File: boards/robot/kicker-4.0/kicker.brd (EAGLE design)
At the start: 141 x 146.1 mm, 157 parts, among them J1 B2PS-VH(LF)(SN), J2 B2PS-VH(LF)(SN), J3 B2PS-VH(LF)(SN), J4 HFW8R-1ST, J5 2-PIN_2MM-H, J6 3-PIN_2MM-H, J7 !BTN_KCK_PRE_EXT, J8 !BTN_CHP_PRE_EXT, J9 !BTN_CHG_PRE_EXT, Q1 ATP302ATPAK, Q10 BSS806NSOT-23-3, Q2 IRFS4227, Q3 IXGK400N30A3, Q4 IXGK400N30A3, Q5 BSS127, Q6 AOD1N60, Q7 BSS127, Q8 BSS127, Q9 BSS127, T1 DA203X-ALDA2034, U1 MPM3620GQV-P, U2 15V, U3 LT3751FE, U4 IX4427N, U5 AT32ATQFP44, U6 ADUM7441ARQZ-RL7, U7 ADUM7441CRQZ-RL7

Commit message: Fixed buttons
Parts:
- removed J7: !BTN_KCK_PRE_EXT, RoboJackets-Connectors:1X2
- removed J8: !BTN_CHP_PRE_EXT, RoboJackets-Connectors:1X2
- removed J9: !BTN_CHG_PRE_EXT, RoboJackets-Connectors:1X2
- S2, S3, S4: value HDP001R -> KMR2; device RoboJackets-Switches:HDP001R -> RoboJackets-Switches:KMR2
- moved S3 1.12 mm to (68.0, -8.00), turned to 90 degrees
- moved R52 1.00 mm to (57.2, -4.40)
- moved S2 0.71 mm to (68.0, 2.00), turned to 90 degrees
- moved S4 0.71 mm to (68.0, -19.0), turned to 90 degrees
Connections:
- net !BTN_CHG: now also S4.2.1, S4.2.2; no longer J9.1, S4.C
- net !BTN_CHP: now also S2.2.1, S2.2.2; no longer J8.1, S2.C
- net !BTN_KCK: now also S3.2.1, S3.2.2; no longer J7.1, S3.C
- net GND: now also S2.1.1, S2.1.2, S3.1.1, S3.1.2, S4.1.1, S4.1.2; no longer J7.2, J8.2, J9.2, S2.B, S3.B, S4.B
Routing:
- net GND: track 220.2 -> 232.2 mm
- net !BTN_KCK: track 52.6 -> 59.4 mm, vias 3 -> 4
- net !BTN_CHG: track 60.1 -> 66.1 mm, vias 3 -> 4
- net !BTN_CHP: track 28.0 -> 31.3 mm
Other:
- board text added: "18.5V"
- board text removed: "PWR: 16-22V"

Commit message: Pot moved
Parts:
- moved RV1 40.2 mm to (-4.20, 74.5), turned to 0 degrees
- moved Q7 5.83 mm to (-1.80, 69.1)
- moved R48 3.61 mm to (34.0, 61.9)
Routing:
- net N$3: track 1.65 -> 49.7 mm
- net +5V: track 232.7 -> 256.2 mm, vias 6 -> 8
- net !DONE!_RAW: track 270.6 -> 276.0 mm
- net BB_TX_CL: track 6.83 -> 3.58 mm
- net GND: track 232.2 -> 233.4 mm
- net N$37: track 14.3 -> 13.3 mm

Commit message: More fixes
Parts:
- added C39, C40, C41: 0.1uF 25V, rcl:C0603
- J4: value HFW8R-1ST -> SFW8R-1STE1LF; device RoboJackets-Connectors:HFW8R-1ST -> RoboJackets-Connectors:SFW8R-1STE1LF
- R12: value 1.02k 1% -> 1k 0.1%
- R13: value 11.5k 1% -> 11.5k 0.1%
- R14: value 25.5k 1% -> 25.5k 0.1%
- R16: value 7m 1% >1W -> 10m 0.1% >1W
- R18: value 113k 0.1% -> 114k 0.1%
- R19: value 3.0k 0.1% -> 3.12k 0.1%
- R20, R21, R24: value 100k -> 10k
- R22, R23, R25, R28, R29: value 160 -> 1k
- R30: value 270k -> 300k
- R34: value 1.5k 35W -> 1.0k 3.5W
- R46: value ERJ-P06J274V -> ERJ-P06J140V
- XF1: value 15A -> 10A
- moved C34 10.1 mm to (55.6, 36.4), flipped to the bottom, turned to 0 degrees
- moved J4 6.08 mm to (68.0, 33.0)
- moved S1 1.41 mm to (64.0, 52.0)
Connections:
- net !BTN_CHG: now also C41.1
- net !BTN_CHP: now also C39.1
- net !BTN_KCK: now also C40.1
- net !KICKER_SELECT_EXT: now also J4.P$6; no longer J4.5
- net !RESET_EXT: now also J4.P$5; no longer J4.4
- net GND: now also C39.2, C40.2, C41.2
- net GND_LGC_EXT: now also J4.P$4; no longer J4.3
- net MISO_EXT: now also J4.P$9; no longer J4.8
- net MOSI_EXT: now also J4.P$8; no longer J4.7
- net SCK_EXT: now also J4.P$7; no longer J4.6
- net VCC_LGC_EXT: now also J4.P$3; no longer J4.2
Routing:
- net VCC_LGC_EXT: track 35.4 -> 43.2 mm, vias 0 -> 1
- net GND: track 233.4 -> 237.1 mm, vias 372 -> 374
- net !BTN_CHP: track 31.3 -> 34.2 mm
- net !BTN_CHG: track 66.1 -> 68.4 mm
- net !BTN_KCK: track 59.3 -> 61.2 mm
- net !RESET_EXT: track 8.89 -> 7.77 mm
- net GND_LGC_EXT: track 27.9 -> 27.0 mm
- net N$14: track 3.30 -> 3.89 mm
- net +5V: track 256.2 -> 255.6 mm

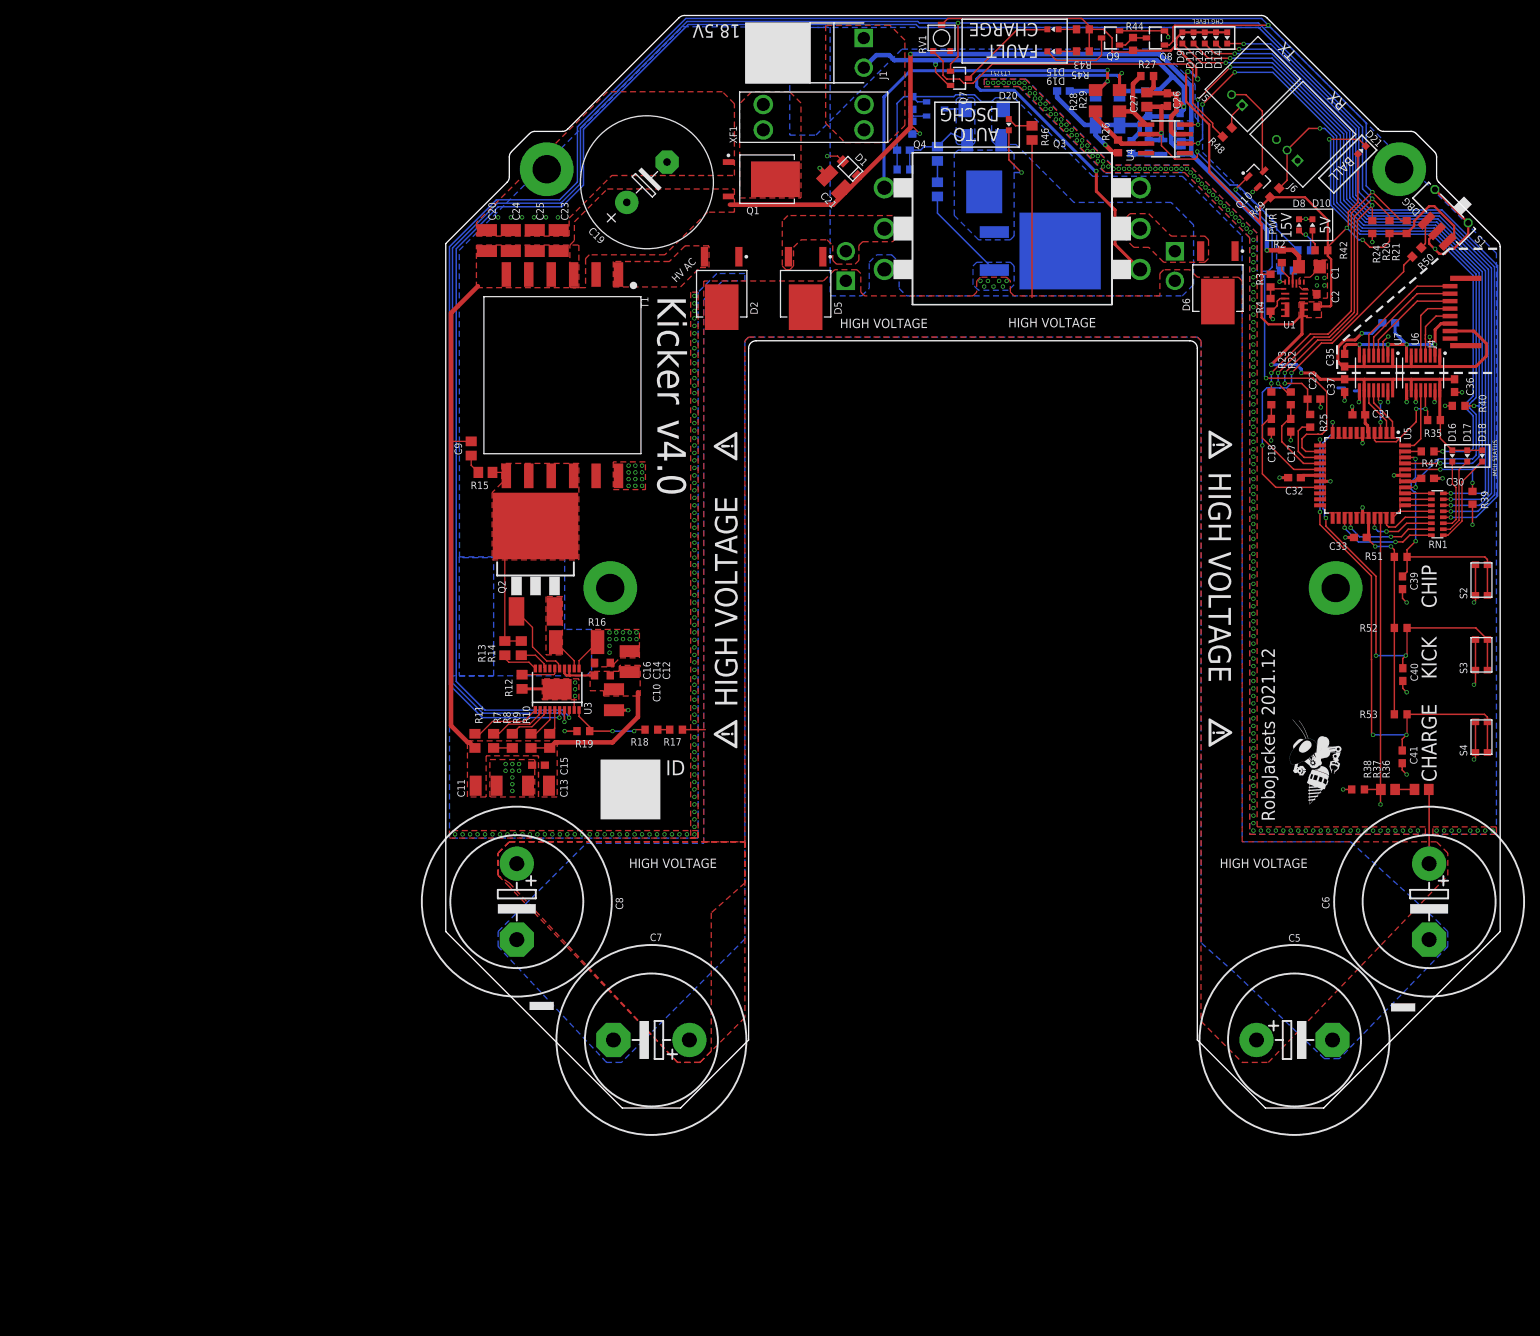
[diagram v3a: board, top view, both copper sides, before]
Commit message: Moved solenoid connectors
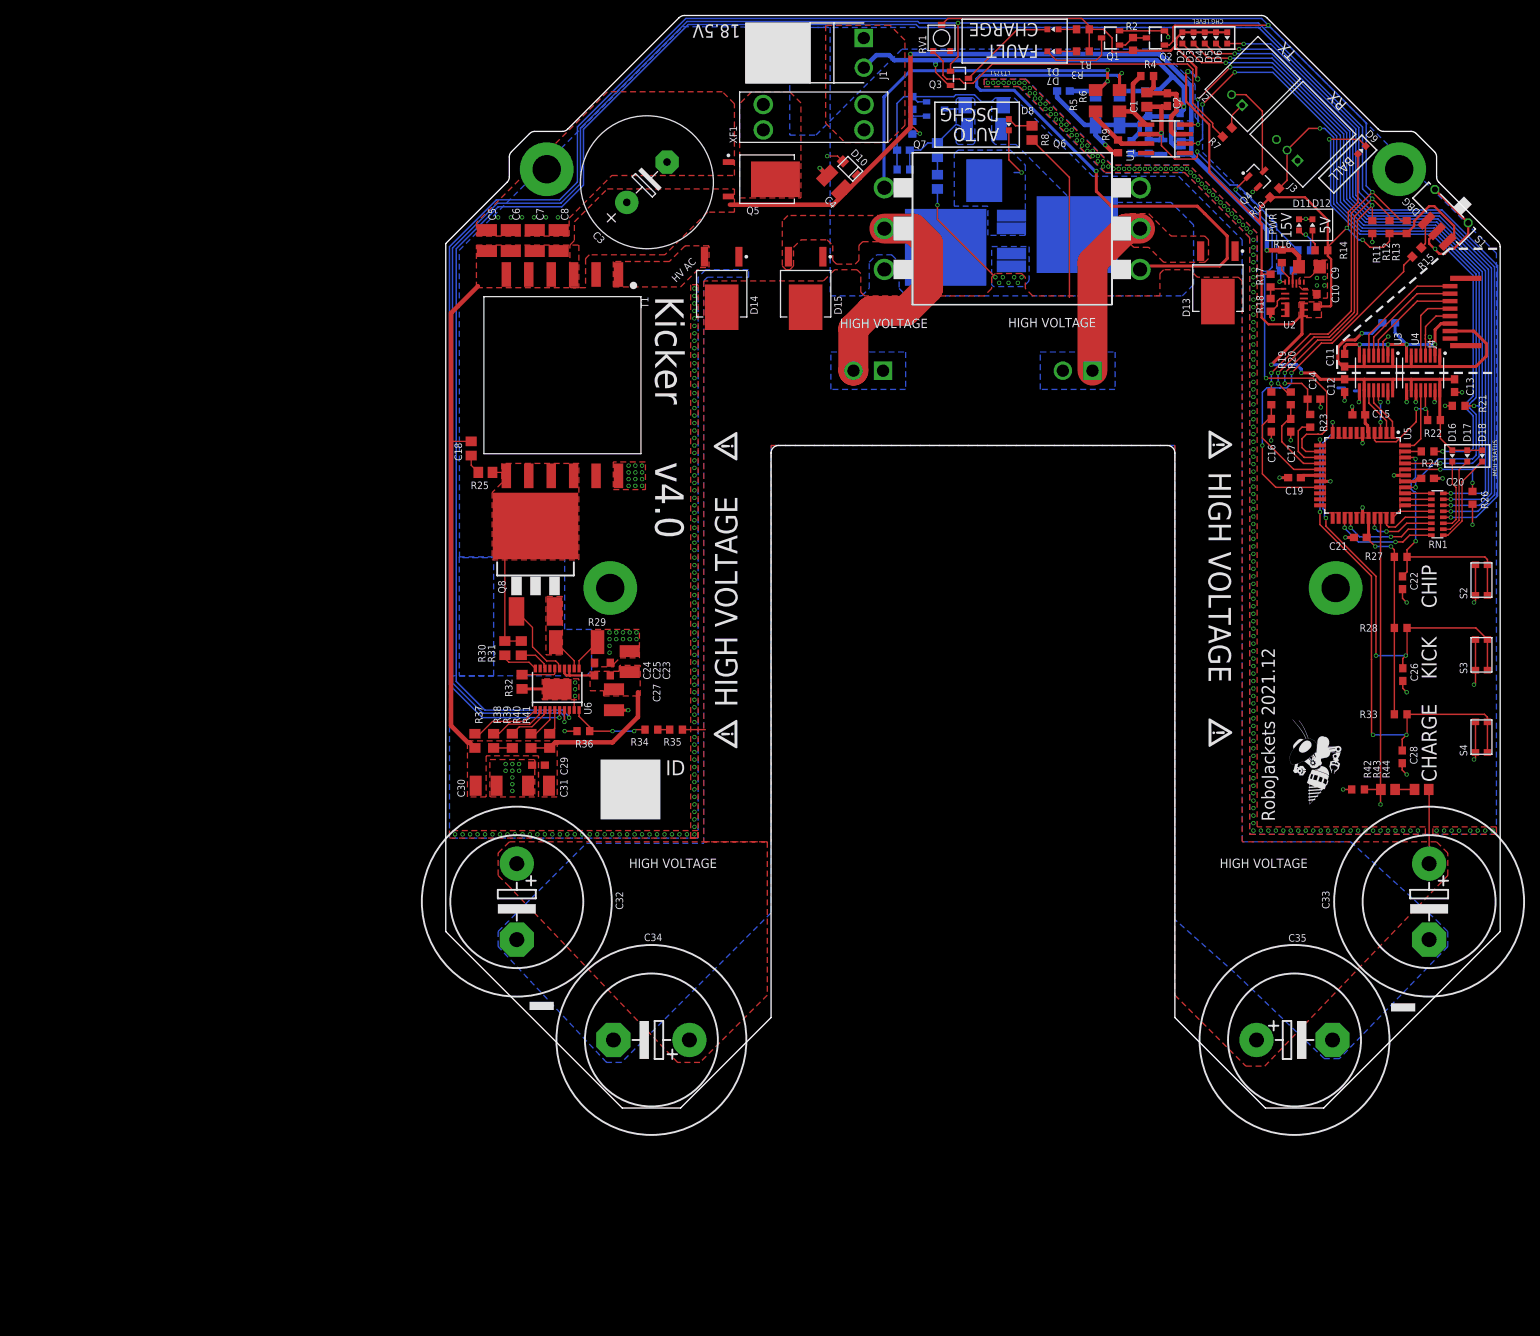
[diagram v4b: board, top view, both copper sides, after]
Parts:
- removed C36, C37: 0.1uF, rcl:C0603
- removed C39, C40, C41: 0.1uF 25V, rcl:C0603
- removed D19: RED, RoboJackets-LEDs:CHIP-LED0603
- removed D20: YELLOW, RoboJackets-LEDs:CHIP-LED0603
- removed D21: BLUE, RoboJackets-LEDs:CHIP-LED0603
- removed J5: 2-PIN_2MM-H, RoboJackets-Connectors:2MM-2-H
- removed J6: 3-PIN_2MM-H, RoboJackets-Connectors:2MM-3-H
- removed Q10: BSS806NSOT-23-3, RoboJackets-Discrete:SOT95P240X110-3
- removed Q9: BSS127, RoboJackets-Discrete:SOT-23-3
- removed R45: 330, rcl:R0603
- removed R46: ERJ-P06J140V, rcl:R0805
- removed R47: 160, rcl:R0603
- removed R48: 51, rcl:R0603
- removed R49, R50, R51, R52, R53: 10k, rcl:R0603
- removed U7: ADUM7441CRQZ-RL7, RoboJackets-ICs:SOP63P574X165-16
- added C100: 0.1uF, rcl:C0603
- added C102: 2.2uF 35V, rcl:C0603
- added C103: 1uF 50V, rcl:C0603
- added C104, C105: 0.1uF 50V, rcl:C0603
- added D100, D101: SMAJ20A, RoboJackets-Diodes:RESM5226X262
- added D102: 3SMBJ5929B-TP, RoboJackets-Diodes:DO214AA
- added J100, J101: B2PS-VH(LF)(SN), RoboJackets-Connectors:B2PS-CENTERED
- added Q100: AOD1N60, RoboJackets-Discrete:DPAK
- added Q101: BSS127, RoboJackets-Discrete:SOT-23-3
- added R100: 43.2k 1%, rcl:R0603
- added R101: 1k, rcl:R0603
- added R102, R103: 1.0k 3.5W, RoboJackets-Resistors:TO508P1539X450-3
- added R104, R106: ERJ-6GEYJ515V, rcl:R0805
- added R107: 110k 1%, rcl:R0603
- added R108: 10k 1%, rcl:R0603
- added R109: 300k, rcl:R0603
- added R110: 100k, rcl:R0603
- added U100: 15V, RoboJackets-PowerICs:SOT95P280X145-5
- C1: value 10uF 50V -> 22uF 35V; device rcl:C1206 -> rcl:C0805
- C10: value 10uF (X7R) 35V -> 22uF 10V; device rcl:C1210 -> rcl:C0603
- C11, C12, C13: value 10uF (X7R) 35V -> 0.1uF; device rcl:C1210 -> rcl:C0603
- C14, C16: value 0.1uF 35V -> 1uF
- C15: value 0.1uF 35V -> 0.1uF
- C18: value 1uF -> 220pF 100V; device rcl:C0603 -> rcl:C0805
- C19: value 560uF -> 0.1uF; device rcl:E7,5-18 -> rcl:C0603
- C2: value 22uF 10V -> 0.1uF 35V
- C20, C21: value 10uF (X7R) -> 0.1uF; device rcl:C1210 -> rcl:C0603
- C22: value 1uF -> 0.1uF 25V
- C23: value 10uF (X7R) -> 10uF (X7R) 35V
- C24, C25: value 10uF (X7R) -> 0.1uF 35V; device rcl:C1210 -> rcl:C0603
- C26: value 0.1uF 35V -> 0.1uF 25V
- C27: value 22uF 35V -> 10uF (X7R) 35V; device rcl:C0805 -> rcl:C1210
- C28: value 0.1uF 50V -> 0.1uF 25V
- C29: value 0.1uF 50V -> 0.1uF 35V
- C3: value 1uF 50V -> 560uF; device rcl:C0603 -> rcl:E7,5-18
- C30, C31: value 0.1uF -> 10uF (X7R) 35V; device rcl:C0603 -> rcl:C1210
- C32, C33, C34, C35: value 0.1uF -> 1000uF; device rcl:C0603 -> rcl:EB25D
- C4: value 2.2uF 35V -> 10uF (X7R); device rcl:C0603 -> rcl:C1210
- C5, C6, C7, C8: value 1000uF -> 10uF (X7R); device rcl:EB25D -> rcl:C1210
- C9: value 220pF 100V -> 10uF 50V; device rcl:C0805 -> rcl:C1206
- D1: value PTVS20VS1UR -> GREEN; device RoboJackets-Diodes:SOD123-W -> RoboJackets-LEDs:CHIP-LED0603
- D10: value GREEN -> PTVS20VS1UR; device RoboJackets-LEDs:CHIP-LED0603 -> RoboJackets-Diodes:SOD123-W
- D11: value RED -> GREEN
- D12: value YELLOW -> GREEN
- D13: value YELLOW -> VS-5EWH06FN-M3; device RoboJackets-LEDs:CHIP-LED0603 -> RoboJackets-Diodes:TO460P990X239-3
- D14: value BLUE -> VS-5EWH06FN-M3; device RoboJackets-LEDs:CHIP-LED0603 -> RoboJackets-Diodes:TO460P990X239-3
- D15: value GREEN -> VS-5EWH06FN-M3; device RoboJackets-LEDs:CHIP-LED0603 -> RoboJackets-Diodes:TO460P990X239-3
- D2: value VS-5EWH06FN-M3 -> RED; device RoboJackets-Diodes:TO460P990X239-3 -> RoboJackets-LEDs:CHIP-LED0603
- D3: value SMAJ20A -> RED; device RoboJackets-Diodes:RESM5226X262 -> RoboJackets-LEDs:CHIP-LED0603
- D4: value SMAJ20A -> YELLOW; device RoboJackets-Diodes:RESM5226X262 -> RoboJackets-LEDs:CHIP-LED0603
- D5: value VS-5EWH06FN-M3 -> YELLOW; device RoboJackets-Diodes:TO460P990X239-3 -> RoboJackets-LEDs:CHIP-LED0603
- D6: value VS-5EWH06FN-M3 -> BLUE; device RoboJackets-Diodes:TO460P990X239-3 -> RoboJackets-LEDs:CHIP-LED0603
- D7: value 3SMBJ5929B-TP -> RED; device RoboJackets-Diodes:DO214AA -> RoboJackets-LEDs:CHIP-LED0603
- D8: value GREEN -> YELLOW
- D9: value RED -> BLUE
- J2: value B2PS-VH(LF)(SN) -> 2-PIN_2MM-H; device RoboJackets-Connectors:B2PS-CENTERED -> RoboJackets-Connectors:2MM-2-H
- J3: value B2PS-VH(LF)(SN) -> 3-PIN_2MM-H; device RoboJackets-Connectors:B2PS-CENTERED -> RoboJackets-Connectors:2MM-3-H
- Q1: value ATP302ATPAK -> BSS127; device RoboJackets-Discrete:TO460P950X150-3 -> RoboJackets-Discrete:SOT-23-3
- Q2: value IRFS4227 -> BSS127; device RoboJackets-Discrete:D2PAK -> RoboJackets-Discrete:SOT-23-3
- Q3: value IXGK400N30A3 -> BSS127; device RoboJackets-Discrete:TO264 -> RoboJackets-Discrete:SOT-23-3
- Q4: value IXGK400N30A3 -> BSS806NSOT-23-3; device RoboJackets-Discrete:TO264 -> RoboJackets-Discrete:SOT95P240X110-3
- Q5: value BSS127 -> ATP302ATPAK; device RoboJackets-Discrete:SOT-23-3 -> RoboJackets-Discrete:TO460P950X150-3
- Q6: value AOD1N60 -> IXGK400N30A3; device RoboJackets-Discrete:DPAK -> RoboJackets-Discrete:TO264
- Q7: value BSS127 -> IXGK400N30A3; device RoboJackets-Discrete:SOT-23-3 -> RoboJackets-Discrete:TO264
- Q8: value BSS127 -> IRFS4227; device RoboJackets-Discrete:SOT-23-3 -> RoboJackets-Discrete:D2PAK
- R1: value 43.2k 1% -> 330
- R10: value 412k 1% -> 10k; device rcl:R0805 -> rcl:R0603
- R11: value 25.5k 1% -> 10k; device rcl:R0805 -> rcl:R0603
- R12: value 1k 0.1% -> 10k; device rcl:R0805 -> rcl:R0603
- R13: value 11.5k 0.1% -> 10k; device rcl:R0805 -> rcl:R0603
- R14: value 25.5k 0.1% -> 330; device rcl:R0805 -> rcl:R0603
- R15: value 22 -> 10k; device rcl:R0805 -> rcl:R0603
- R16: value 10m 0.1% >1W -> 100k; device rcl:R2512 -> rcl:R0603
- R17: value 505k 0.1% -> 160k 1%
- R18: value 114k 0.1% -> 30.1k 1%
- R19: value 3.12k 0.1% -> 1k
- R2: value 100k -> 1k
- R20: value 10k -> 1k
- R22: value 1k -> 10k
- R24: value 10k -> 160
- R25: value 1k -> 22; device rcl:R0603 -> rcl:R0805
- R28: value 1k -> 10k; device rcl:R1206 -> rcl:R0603
- R29: value 1k -> 10m 0.1% >1W; device rcl:R1206 -> rcl:R2512
- R3: value 160k 1% -> 330
- R30: value 300k -> 11.5k 0.1%; device rcl:R0603 -> rcl:R0805
- R31: value 100k -> 25.5k 0.1%; device rcl:R0603 -> rcl:R0805
- R32: value ERJ-6GEYJ515V -> 1k 0.1%
- R33: value ERJ-6GEYJ515V -> 10k; device rcl:R0805 -> rcl:R0603
- R34: value 1.0k 3.5W -> 114k 0.1%; device RoboJackets-Resistors:TO508P1539X450-3 -> rcl:R0603
- R35: value 10k -> 505k 0.1%
- R36: value ERJ-6GEYJ515V -> 3.12k 0.1%; device rcl:R0805 -> rcl:R0603
- R37: value ERJ-6GEYJ515V -> 25.5k 1%
- R38: value RC0603FR-07102KL -> 294k 1%; device rcl:R0603 -> rcl:R0805
- R39: value 10k -> 412k 1%; device rcl:R0603 -> rcl:R0805
- R4: value 30.1k 1% -> 10k
- R40: value 10k -> 294k 1%; device rcl:R0603 -> rcl:R0805
- R41: value 1k -> 412k 1%; device rcl:R0603 -> rcl:R0805
- R42: value 330 -> RC0603FR-07102KL
- R43: value 330 -> ERJ-6GEYJ515V; device rcl:R0603 -> rcl:R0805
- R44: value 1k -> ERJ-6GEYJ515V; device rcl:R0603 -> rcl:R0805
- R5: value 110k 1% -> 1k; device rcl:R0603 -> rcl:R1206
- R6: value 10k 1% -> 1k; device rcl:R0603 -> rcl:R1206
- R7: value 294k 1% -> 51; device rcl:R0805 -> rcl:R0603
- R8: value 412k 1% -> ERJ-P06J140V
- R9: value 294k 1% -> 10k; device rcl:R0805 -> rcl:R0603
- U1: value MPM3620GQV-P -> IX4427N; device RoboJackets-PowerICs:MPM3620GQV-P -> RoboJackets-PowerICs:SOIC-8
- U2: value 15V -> MPM3620GQV-P; device RoboJackets-PowerICs:SOT95P280X145-5 -> RoboJackets-PowerICs:MPM3620GQV-P
- U3: value LT3751FE -> ADUM7441CRQZ-RL7; device RoboJackets-ICs:TSSOP-20_EP -> RoboJackets-ICs:SOP63P574X165-16
- U4: value IX4427N -> ADUM7441ARQZ-RL7; device RoboJackets-PowerICs:SOIC-8 -> RoboJackets-ICs:SOP63P574X165-16
- U6: value ADUM7441ARQZ-RL7 -> LT3751FE; device RoboJackets-ICs:SOP63P574X165-16 -> RoboJackets-ICs:TSSOP-20_EP
- moved C5 152.0 mm to (-65.0, 47.4), turned to 90 degrees
- moved C6 151.3 mm to (-61.8, 47.4), turned to 90 degrees
- moved R11 138.3 mm to (53.4, 49.2), turned to 90 degrees
- moved C34 137.5 mm to (-43.0, -59.5), flipped to the top, turned to 180 degrees
- moved C13 133.7 mm to (64.4, 28.0), turned to 90 degrees
- moved R13 133.1 mm to (58.0, 49.2)
- moved R39 132.4 mm to (-61.6, -19.5)
- moved C30 132.4 mm to (-65.1, -25.5), turned to 0 degrees
- moved R40 131.9 mm to (-59.1, -19.5), turned to 90 degrees
- moved R12 131.0 mm to (55.7, 49.2)
- moved C20 129.8 mm to (60.8, 15.6), turned to 180 degrees
- moved C11 128.1 mm to (49.7, 31.4), turned to 270 degrees
- moved R15 128.0 mm to (59.4, 45.9), turned to 225 degrees
- moved R7 127.5 mm to (34.0, 61.9), turned to 45 degrees
- moved U6 123.3 mm to (-55.6, -12.6), turned to 90 degrees
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- renumbered C38 to C101, R54 to R105, U$10 to U$100, U$6 to U$101, U$7 to U$103, U$8 to U$104, U$9 to U$102
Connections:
- net !BTN_CHG: now also C28.1, R33.1; no longer C41.1, R53.1
- net !BTN_CHP: now also C22.1, R27.1; no longer C39.1, R51.1
- net !BTN_KCK: now also C26.1, R28.1; no longer C40.1, R52.1
- net !DONE!: now also R20.1; no longer R22.1
- net !DONE!_RAW: now also Q3.1, R12.1, R20.2, U6.7; no longer Q7.1, R20.1, R22.2, U3.7
- net !FAULT!: now also C16.1, R19.1; no longer C18.1, R23.1
- net !FAULT!_RAW: now also Q2.1, R13.1, R19.2, U6.6; no longer Q8.1, R21.1, R23.2, U3.6
- net !KICKER_SELECT: now also U4.12; no longer U6.12
- net !KICKER_SELECT_EXT: now also U4.5; no longer U6.5
- net !RESET: now also R22.1, U4.13; no longer R35.1, U6.13
- net !RESET_EXT: now also U4.4; no longer U6.4
- net +15.0V: now also C1.2, C102.1, C2.2, R101.2, R107.2, U1.6, U100.5; no longer C26.2, C27.2, C4.1, R41.2, R5.2, U2.5, U4.6
- net +5V: now also C10.1, C12.2, C13.2, C15.2, C19.2, C20.2, C21.2, D2.A, D3.A, D4.A, D5.A, D6.A, R1.2, R10.2, R12.2, R13.2, R14.2, R17.2, R2.2, R22.2, R27.2, R28.2, R33.2, U2.789, U3.10, U3.16, U4.10, U4.16; no longer C2.1, C30.2, C31.2, C32.2, C33.2, C36.2, C37.2, D11.A, D12.A, D13.A, D14.A, D21.A, R20.2, R21.2, R35.2, R42.2, R43.2, R44.2, R45.2, R49.2, R51.2, R52.2, R53.2, U1.789, U6.10, U6.16, U7.10, U7.16
- net 15V_PWR_BR: now also D11.A, R101.1; no longer D8.A, R41.1
- net BALL_SENSE: now also R24.2; no longer R47.2
- net BALL_SENSE_CL: now also D9.C, R24.1; no longer D21.C, R47.1
- net BB_RX: now also J3.2, R10.1; no longer J6.2, R49.1
- net BB_TX: now also Q4.1; no longer Q10.1
- net BB_TX_CL: now also J2.1, R7.2; no longer J5.1, R48.2
- net CHARGE: now also R23.1; no longer R25.1
- net CHARGE_RAW: now also C14.1, R11.2, R23.2, U6.8; no longer C22.1, R24.2, R25.2, U3.8
- net CHIP: now also R21.2, U1.2; no longer R40.2, U4.2
- net CHIPPER: now also D15.2, J101.2, Q6.C_BOT; no longer D5.2, J2.2, Q3.C_BOT
- net CHIP_GATE: now also R5.1, R9.2, U1.7; no longer R26.2, R28.1, U4.7
- net CHIP_GATE_S: now also C105.1, D101.2, Q6.G_BOT, R5.2; no longer C28.1, D3.2, Q3.G_BOT, R28.2
- net CSP: now also Q8.3, R29.2, U6.12; no longer Q2.3, R16.2, U3.12
- net DISCHARGE_DRAIN: now also D8.C, Q100.4, R102.1, R103.2; no longer D20.C, Q6.4, R34.2
- net FAULT_INV_BR: now also Q1.1, Q2.3, R2.1; no longer Q8.3, Q9.1, R44.1
- net FB: now also R17.1, R18.2, U2.1; no longer R3.1, R4.2, U1.1
- net GND: now also C1.1, C102.2, C103.2, C104.2, C105.2, C12.1, C13.1, C15.1, C19.1, C2.1, C20.1, C21.1, C26.2, C27.2, C3.-, C30.2, C31.2, C32.-, C33.-, C34.-, C35.-, C5.2, C6.2, C7.2, C8.2, C9.2, D10.A, D100.1, D101.1, D102.A, D11.C, D12.C, J3.1, J3.3, Q1.2, Q100.3, Q101.2, Q2.2, Q3.2, Q4.2, Q5.1, Q6.E_BOT, Q7.E_BOT, R100.1, R108.1, R11.1, R110.1, R18.1, R21.1, R29.1, R32.2, R36.2, R42.1, R9.1, U100.2, U2.12, U2.13, U2.14, U2.3, U3.15, U3.3, U4.11, U4.15, U4.9, U6.PAD; no longer C1.2, C11.2, C12.2, C13.2, C15.2, C18.2, C19.-, C2.2, C20.2, C21.2, C26.1, C27.1, C3.2, C30.1, C31.1, C32.1, C33.1, C36.1, C37.1, C39.2, C40.2, C41.2, C5.-, C6.-, C7.-, C8.-, D1.A, D10.C, D3.1, D4.1, D7.A, D8.C, J6.1, J6.3, Q1.1, Q10.2, Q3.E_BOT, Q4.E_BOT, Q5.2, Q6.3, Q7.2, Q8.2, Q9.2, R1.1, R12.2, R16.1, R19.2, R24.1, R27.1, R31.1, R38.1, R39.1, R40.1, R6.1, U1.12, U1.13, U1.14, U2.2, U3.11, U3.PAD, U6.15, U6.3, U7.15, U7.3, U7.9
- net GND_LGC_EXT: now also C100.1, C11.1, U3.2, U3.8, U4.2, U4.8; no longer C34.1, C35.1, U6.2, U6.8, U7.2, U7.8
- net HVGATE: now also Q8.1, U6.15; no longer Q2.1, U3.15
- net HV_AC: now also D14.2; no longer D2.2
- net HV_FB: now also R34.2, R36.1, U6.10; no longer R18.2, R19.1, U3.10
- net HV_IND_HIGH_CL: now also D3.C; no longer D11.C
- net HV_IND_LOW_CL: now also D5.C; no longer D13.C
- net HV_IND_MAX_CL: now also D2.C; no longer D9.C
- net HV_IND_MID_CL: now also D4.C; no longer D12.C
- net HV_IND_MIN_CL: now also D6.C; no longer D14.C
- net HV_SENSE_DIV_BR: now also R43.2, R44.1; no longer R36.1, R37.2
- net KICK: now also R26.2, U1.4; no longer R39.2, U4.4
- net KICKER: now also D13.2, J100.1, Q7.C_BOT; no longer D6.2, J3.1, Q4.C_BOT
- net KICK_GATE: now also R4.2, R6.1, U1.5; no longer R27.2, R29.1, U4.5
- net KICK_GATE_S: now also C104.1, D100.2, Q7.G_BOT, R6.2; no longer C29.1, D4.2, Q4.G_BOT, R29.2
- net MISO: now also U3.11; no longer U7.11
- net MISO_EXT: now also U3.6; no longer U7.6
- net MODE_SELECT: now also R15.2; no longer R50.2
- net MOSI: now also U3.12; no longer U7.12
- net MOSI_EXT: now also U3.5; no longer U7.5
- net N$1: now also R32.1, U6.16; no longer R12.1, U3.16
- net N$14: now also R15.1; no longer R50.1
- net N$16: now also R107.1, R108.2, U100.4; no longer R5.1, R6.2, U2.4
- net N$18: now also C18.1, R25.2; no longer C9.1, R15.2
- net N$19: now also J2.2, Q4.3; no longer J5.2, Q10.3
- net N$2: now also R34.1, R35.2; no longer R17.2, R18.1
- net N$20: now also D12.A, R14.1; no longer D10.A, R42.1
- net N$24: now also R37.1, U6.1; no longer R11.1, U3.1
- net N$27: now also D7.A, R3.1; no longer D19.A, R45.1
- net N$28: now also D7.C, Q1.3; no longer D19.C, Q9.3
- net N$29: now also D8.A, R8.1; no longer D20.A, R46.1
- net N$3: now also R7.1; no longer R48.1
- net N$37: now also D1.C, Q3.3; no longer D15.C, Q7.3
- net N$5: now also D1.A, R1.1; no longer D15.A, R43.1
- net N$9: now also Q5.3; no longer Q1.3
- net OVLO1: now also R39.2, U6.3; no longer R8.2, U3.3
- net OVLO2: now also R41.2, U6.5; no longer R10.2, U3.5
- net QD_GATE_CTRL: now also Q101.1, R109.1, R110.2; no longer Q5.1, R30.1, R31.2
- net QD_PU_BR: now also R104.1, R106.2; no longer R32.1, R33.2
- net QUICK_DISCHARGE: now also D102.C, Q100.1, Q101.3, R106.1; no longer D7.C, Q5.3, Q6.1, R33.1
- net RDCM: now also R30.2, U6.20; no longer R13.2, U3.20
- net REG_AAM: now also R100.2, U2.18; no longer R1.2, U1.18
- net REG_EN: now also R16.2, U2.17; no longer R2.2, U1.17
- net RVOUT: now also R31.2, U6.18; no longer R14.2, U3.18
- net SCK: now also U3.13; no longer U7.13
- net SCK_EXT: now also U3.4; no longer U7.4
- net UVLO1: now also R38.2, U6.2; no longer R7.2, U3.2
- net UVLO2: now also R40.2, U6.4; no longer R9.2, U3.4
- net V+: now also C32.+, C33.+, C34.+, C35.+, D13.3, D14.3, D15.3, J100.2, J101.1, R102.2, R103.1, R104.2, R35.1, R44.2, R8.2; no longer C5.+, C6.+, C7.+, C8.+, D2.3, D5.3, D6.3, J2.1, J3.2, R17.1, R32.2, R34.1, R36.2, R46.2
- net VBATT: now also C103.1, C18.2, C27.1, C29.1, C3.+, C30.1, C31.1, C4.1, C5.1, C6.1, C7.1, C8.1, C9.1, D10.C, Q5.2, R109.2, R16.1, R37.2, R38.1, R39.1, R40.1, R41.1, U100.1, U100.3, U2.16, U6.13, U6.14; no longer C1.1, C10.1, C11.1, C12.1, C13.1, C14.1, C15.1, C16.1, C19.+, C20.1, C21.1, C3.1, C9.2, D1.C, Q1.2, R10.1, R11.2, R2.1, R30.2, R7.1, R8.1, R9.1, U1.16, U2.1, U2.3, U3.13, U3.14
- net VCC_LGC_EXT: now also C100.2, C11.2, U3.1, U3.7, U4.1, U4.7; no longer C34.2, C35.2, U6.1, U6.7, U7.1, U7.7
- net VMON: now also R42.2, R43.1; no longer R37.1, R38.2
- net VSN: now also Q8.2, R25.1, R30.1, R31.1; no longer Q2.2, R13.1, R14.1, R15.1
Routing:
- net CHIPPER: track 0.00 -> 30.5 mm
- net KICKER: track 0.00 -> 22.7 mm
- net KICK_GATE_S: track 65.4 -> 87.7 mm
- net V+: track 47.0 -> 51.2 mm, vias 7 -> 8
- net QD_PU_BR: track 2.85 -> 2.35 mm
- net GND: vias 374 -> 375
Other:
- outline, holes or cut-outs redrawn
